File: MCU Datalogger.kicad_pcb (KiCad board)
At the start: 4 copper layers, 51.6 x 36 mm, 30 parts, among them J1 Conn_01x04_Pin, J2 Conn_01x09_Pin, J3 Conn_01x04_Pin, J4 Conn_02x03_Odd_Even, U1 24LC1025, U2 DS1337S_, U3 24LC1025, U4 ATMEGA328P-AU, Y1 32.768 KHz, Y2 16 MHz

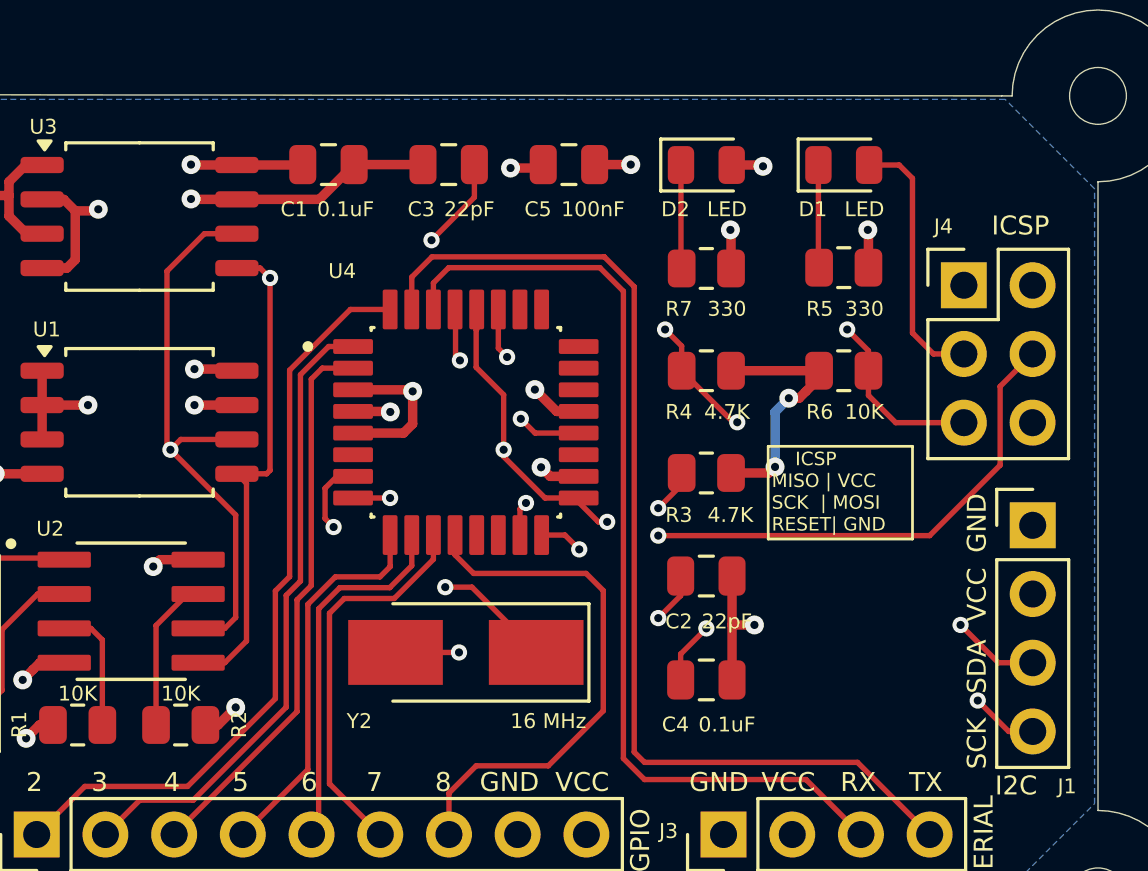
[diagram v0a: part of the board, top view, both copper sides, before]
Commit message: Fixed net bugs in 4 layer version.
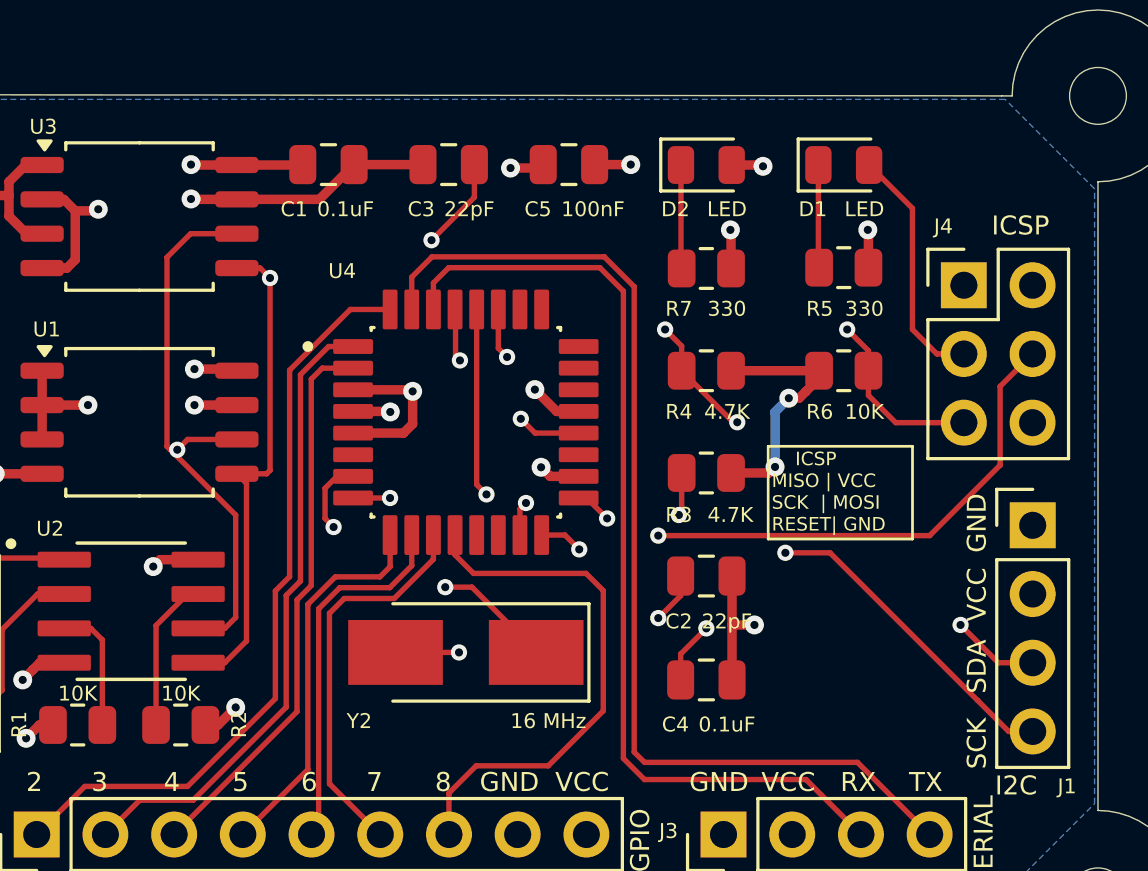
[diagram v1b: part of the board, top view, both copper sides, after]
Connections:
- J1 pad 4: /SCK -> /SCL
- R3 pad 2: /SCK -> /SCL
- U1 pad 6: /SCK -> /SCL
- U2 pad 6: /SCK -> /SCL
- U3 pad 6: /SCK -> /SCL
- U4 pad 28: /SCK -> /SCL
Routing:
- net /SCL: track 0.00 -> 74.6 mm, vias 0 -> 4
- net /SCK: track 89.9 -> 26.1 mm, vias 5 -> 1

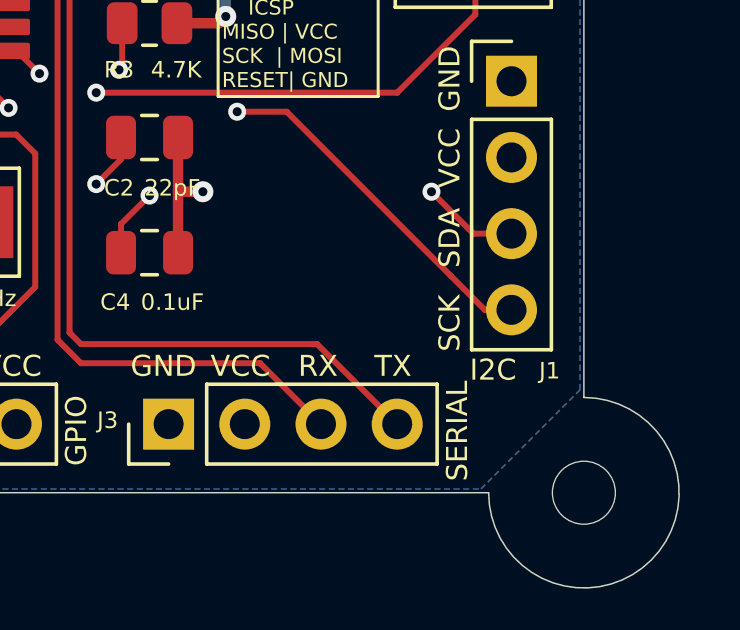
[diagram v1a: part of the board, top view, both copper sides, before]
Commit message: prl file changed after exiting.
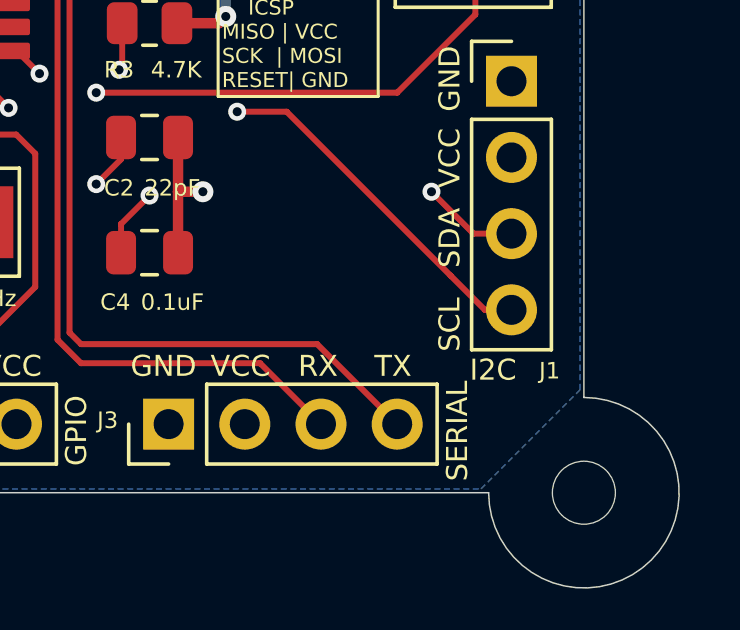
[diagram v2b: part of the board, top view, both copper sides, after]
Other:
- board text added: "SCL"
- board text removed: "SCK"
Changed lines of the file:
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@@
 		)
 	)
-	(gr_text "SCK"
+	(gr_text "SCL"
 		(at 196.469 111.252 90)
 		(layer "F.SilkS")

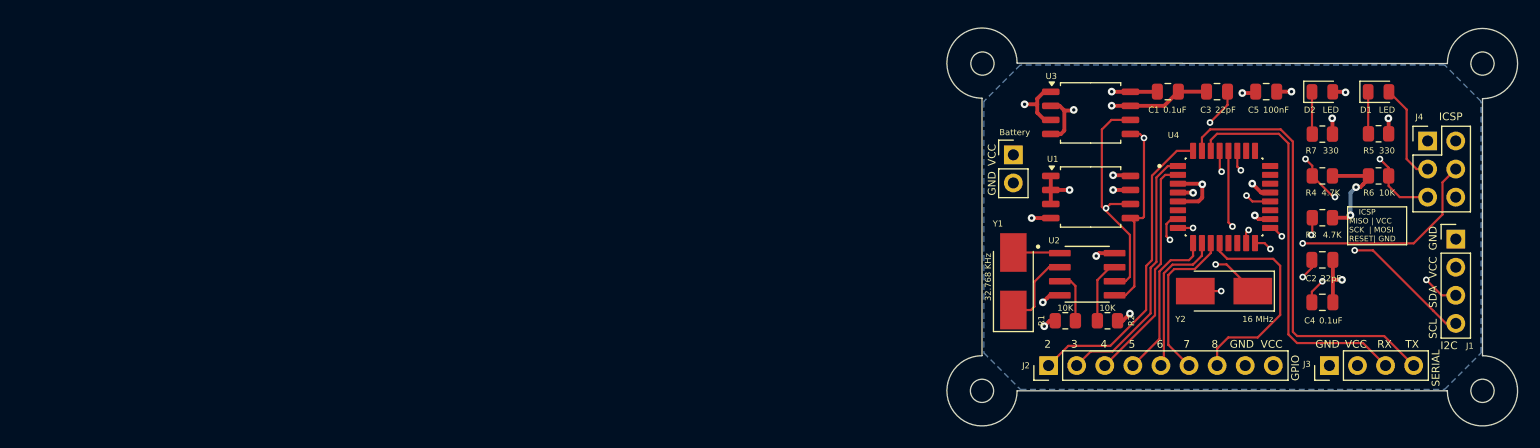
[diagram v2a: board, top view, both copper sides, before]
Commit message: Finished 4layer PCB project.
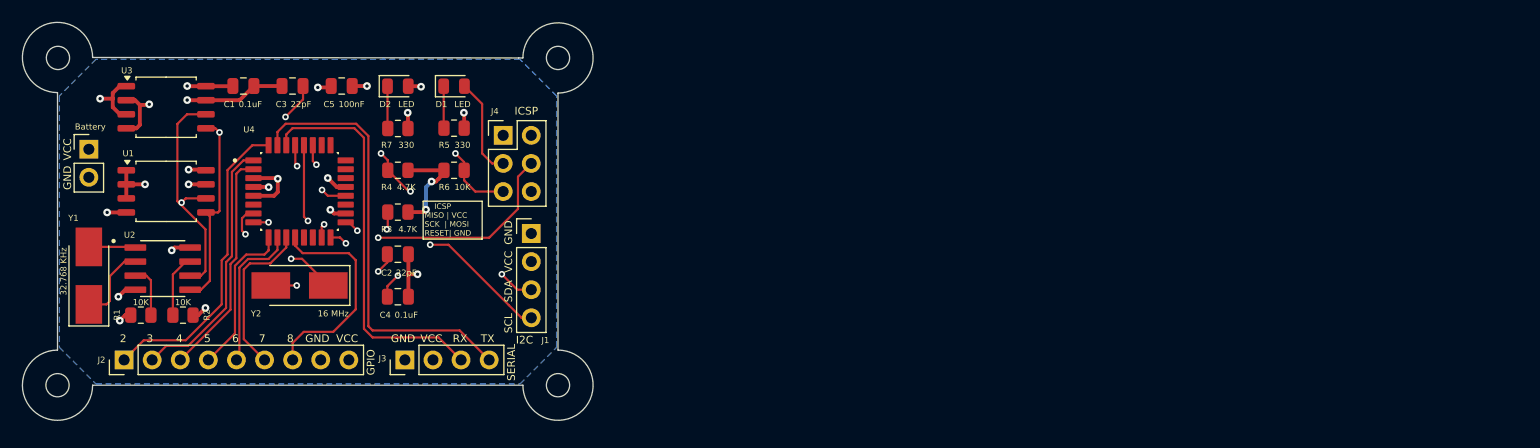
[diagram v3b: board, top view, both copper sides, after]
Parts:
- moved BT1 83.6 mm to (74.5, 94.1)
- moved H2 83.6 mm to (71.7, 115.4)
- moved J2 83.6 mm to (77.7, 113.2)
- moved Y1 83.6 mm to (74.5, 105.5)
- moved C1 83.6 mm to (88.5, 88.4)
- moved C2 83.6 mm to (102.5, 103.6)
- moved C3 83.6 mm to (92.9, 88.4)
- moved C4 83.6 mm to (102.5, 107.4)
- moved C5 83.6 mm to (97.4, 88.4)
- moved D2 83.6 mm to (102.5, 88.4)
- moved H1 83.6 mm to (71.7, 85.9)
- moved J1 83.6 mm to (114.5, 101.7)
- moved J3 83.6 mm to (103.1, 113.2)
- moved R2 83.6 mm to (83.0, 109.1)
- moved R3 83.6 mm to (102.5, 99.8)
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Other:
- board text added: "0.0000 mm / 0.0000 mm"
- board text added: "0.3000 mm"
- board text added: "1.6000 mm"
- board text added: "51.5981 mm x 35.9771 mm"
- board text added: "BOARD CHARACTERISTICS"
- board text added: "Board Thickness:"
- board text added: "Board overall dimensions:"
- board text added: "Castellated pads:"
- board text added: "Copper Finish:"
- board text added: "Copper Layer Count:"
- board text added: "Edge card connectors:"
- board text added: "Impedance Control:"
- board text added: "Min hole diameter:"
- board text added: "Min track/spacing:"
- board text added: "No"
- board text added: "None"
- board text added: "Plated Board Edge:"

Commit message: Added B silkscreen text.
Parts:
- added REF**: KiCad-Logo2_5mm_SilkScreen, Symbol:KiCad-Logo2_5mm_SilkScreen, B.Cu at (94.1, 92.6)
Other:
- board text added: "Data logger with ATMega328P."
